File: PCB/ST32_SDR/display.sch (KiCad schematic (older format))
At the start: 1 part

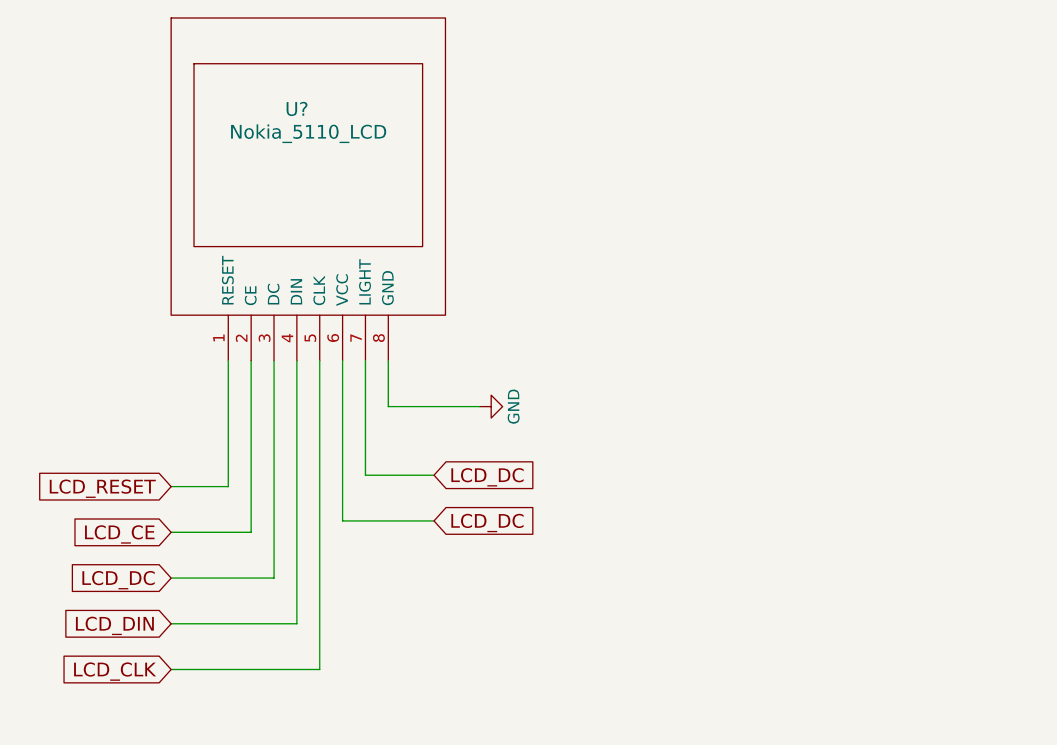
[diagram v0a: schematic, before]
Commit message: add LCD resistors
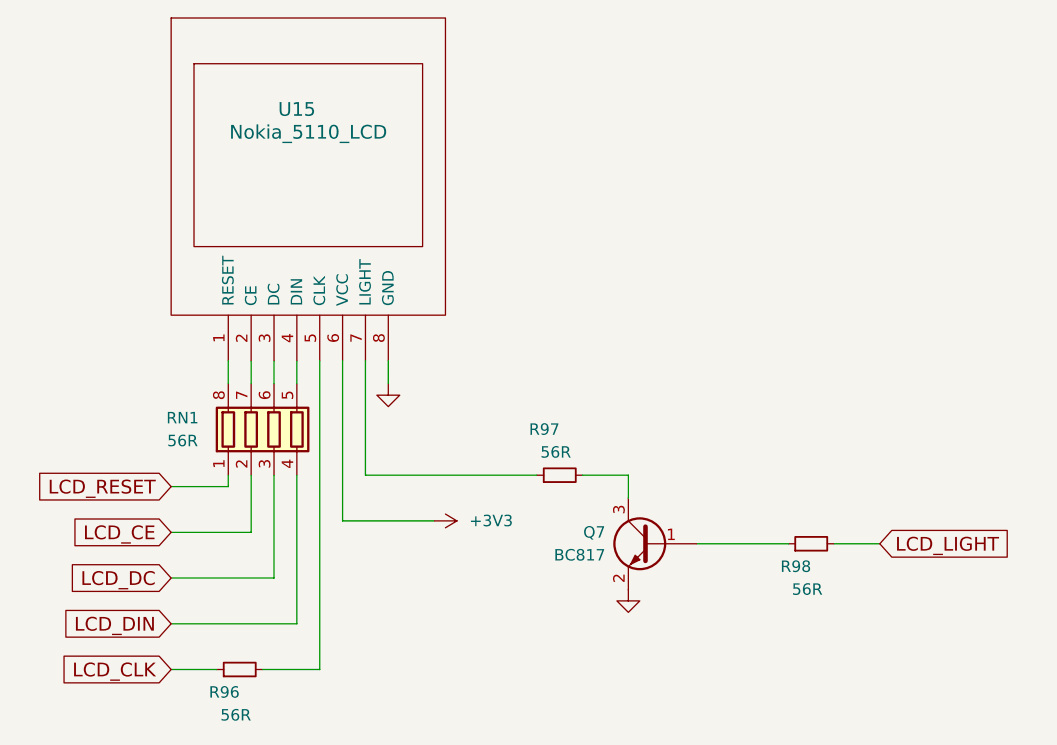
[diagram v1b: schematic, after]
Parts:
- added Q7: BC817, symbol Q_NPN_BEC
- added R96, R97, R98: 56R, symbol R_Small
- added RN1: 56R, symbol R_Pack04
- gave numbers to parts that had none: 1
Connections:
- net GND: now also Q7.2 (E)
- net LCD_CE: now also RN1.2 (R2.1); no longer U15.2 (CE)
- net LCD_CLK: now also R96.1; no longer U15.5 (CLK)
- net LCD_DC: now also RN1.3 (R3.1); no longer U15.3 (DC), U15.6 (VCC), U15.7 (LIGHT)
- net LCD_DIN: now also RN1.4 (R4.1); no longer U15.4 (DIN)
- net LCD_RESET: now also RN1.1 (R1.1); no longer U15.1 (RESET)
- new net: RN1.8 (R1.2), U15.1 (RESET)
- new net: RN1.7 (R2.2), U15.2 (CE)
- new net: RN1.6 (R3.2), U15.3 (DC)
- new net: RN1.5 (R4.2), U15.4 (DIN)
- new net: R96.2, U15.5 (CLK)
- new net: R97.1, U15.7 (LIGHT)
- new net: Q7.1 (B), R98.1
- new net: Q7.3 (C), R97.2
- new net +3V3: U15.6 (VCC)
- new net LCD_LIGHT: R98.2
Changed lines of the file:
@@
 $EndDescr
 $Comp
-L GND #PWR?
+L GND #PWR177
 U 1 1 5DDA30F6
-P 3900 2700
-F 0 "#PWR?" H 3900 2450 50  0001 C CNN
-F 1 "GND" H 3900 2550 50  0000 C CNN
-F 2 "" H 3900 2700 50  0001 C CNN
-F 3 "" H 3900 2700 50  0001 C CNN
-	1    3900 2700
-	0    -1   -1   0
+P 3500 2600
+F 0 "#PWR177" H 3500 2350 50  0001 C CNN
+F 1 "GND" H 3500 2450 50  0001 C CNN
+F 2 "" H 3500 2600 50  0001 C CNN
+F 3 "" H 3500 2600 50  0001 C CNN
+	1    3500 2600
+	1    0    0    -1
 $EndComp
 $Comp
-L Nokia_5110_LCD U?
+L Nokia_5110_LCD U15
 U 1 1 5DDA3747
 P 3150 1600
-F 0 "U?" H 3100 1800 60  0000 C CNN
+F 0 "U15" H 3100 1800 60  0000 C CNN
 F 1 "Nokia_5110_LCD" H 3150 1700 60  0000 C CNN
 F 2 "" H 2700 1400 60  0000 C CNN
@@
 	1    0    0    -1
 $EndComp
-Wire Wire Line
-	3500 2500 3500 2700
-Wire Wire Line
-	3500 2700 3900 2700
-Wire Wire Line
-	3000 2500 3000 3450
 Text GLabel 2550 3450 0    60   Input ~ 0
 LCD_DC
-Wire Wire Line
-	3000 3450 2550 3450
 Text GLabel 2550 3250 0    60   Input ~ 0
 LCD_CE
-Wire Wire Line
-	2550 3250 2900 3250
-Wire Wire Line
-	2900 3250 2900 2500
 Text GLabel 2550 3050 0    60   Input ~ 0
 LCD_RESET
+Text GLabel 2550 3650 0    60   Input ~ 0
+LCD_DIN
+Text GLabel 2550 3850 0    60   Input ~ 0
+LCD_CLK
+Text GLabel 5650 3300 2    60   Input ~ 0
+LCD_LIGHT
+$Comp
+L R_Pack04 RN1
+U 1 1 5DDA5123
+P 3000 2800
+F 0 "RN1" H 2600 2850 50  0000 C CNN
+F 1 "56R" H 2600 2750 50  0000 C CNN
+F 2 "" V 3275 2800 50  0001 C CNN
+F 3 "" H 3000 2800 50  0001 C CNN
+	1    3000 2800
+	1    0    0    -1
+$EndComp
+$Comp
+L +3V3 #PWR178
+U 1 1 5DDA52BE
+P 3700 3200
+F 0 "#PWR178" H 3700 3050 50  0001 C CNN
+F 1 "+3V3" V 3700 3450 50  0000 C CNN
+F 2 "" H 3700 3200 50  0001 C CNN
+F 3 "" H 3700 3200 50  0001 C CNN
+	1    3700 3200
+	0    1    1    0
+$EndComp
 Wire Wire Line
 	2550 3050 2800 3050
 Wire Wire Line
-	2800 3050 2800 2500
-Text GLabel 2550 3650 0    60   Input ~ 0
-LCD_DIN
-Wire Wire Line
 	2550 3650 3100 3650
-Wire Wire Line
-	3100 3650 3100 2500
-Text GLabel 2550 3850 0    60   Input ~ 0
-LCD_CLK
-Wire Wire Line
-	2550 3850 3200 3850
-Wire Wire Line
-	3200 3850 3200 2500
-Text GLabel 3700 3000 2    60   Input ~ 0
-LCD_DC
-Wire Wire Line
-	3700 3000 3400 3000
 Wire Wire Line
 	3400 3000 3400 2500
@@
 Wire Wire Line
 	3300 3200 3700 3200
-Text GLabel 3700 3200 2    60   Input ~ 0
-LCD_DC
+Wire Wire Line
+	3000 3450 2550 3450
+Wire Wire Line
+	2550 3250 2900 3250
+Wire Wire Line
+	2800 2600 2800 2500
+Wire Wire Line
+	2900 2500 2900 2600
+Wire Wire Line
+	3000 2500 3000 2600
+Wire Wire Line
+	3100 2500 3100 2600
+Wire Wire Line
+	3200 3850 3200 2500
+Wire Wire Line
+	2800 3050 2800 3000
+Wire Wire Line
+	2900 3250 2900 3000
+Wire Wire Line
+	3000 3450 3000 3000
+Wire Wire Line
+	3100 3650 3100 3000
+$Comp
+L R_Small R96
+U 1 1 5DDA5492
+P 2850 3850
+F 0 "R96" V 2750 3850 50  0000 L CNN
+F 1 "56R" V 2650 3800 50  0000 L CNN
+F 2 "" H 2850 3850 50  0001 C CNN
+F 3 "" H 2850 3850 50  0001 C CNN
+	1    2850 3850
+	0    -1   -1   0
+$EndComp
+Wire Wire Line
+	2950 3850 3200 3850
+Wire Wire Line
+	2750 3850 2550 3850
+$Comp
+L Q_NPN_BEC Q7
+U 1 1 5DDA55BA
+P 4650 3300
+F 0 "Q7" H 4850 3350 50  0000 L CNN
+F 1 "BC817" H 4850 3250 50  0000 L CNN
+F 2 "" H 4850 3400 50  0001 C CNN
+F 3 "" H 4650 3300 50  0001 C CNN
+	1    4650 3300
+	-1   0    0    -1
+$EndComp
+Wire Wire Line
+	4550 3000 4550 3100
+$Comp
+L R_Small R98
+U 1 1 5DDA5646
+P 5350 3300
+F 0 "R98" V 5250 3300 50  0000 L CNN
+F 1 "56R" V 5150 3250 50  0000 L CNN
+F 2 "" H 5350 3300 50  0001 C CNN
+F 3 "" H 5350 3300 50  0001 C CNN
+	1    5350 3300
+	0    -1   -1   0
+$EndComp
+Wire Wire Line
+	5450 3300 5650 3300
+Wire Wire Line
+	5250 3300 4850 3300
+$Comp
+L GND #PWR179
+U 1 1 5DDA5709
+P 4550 3500
+F 0 "#PWR179" H 4550 3250 50  0001 C CNN
+F 1 "GND" H 4550 3350 50  0001 C CNN
+F 2 "" H 4550 3500 50  0001 C CNN
+F 3 "" H 4550 3500 50  0001 C CNN
+	1    4550 3500
+	1    0    0    -1
+$EndComp
+Wire Wire Line
+	3500 2600 3500 2500
+$Comp
+L R_Small R97
+U 1 1 5DDA5830
+P 4250 3000
+F 0 "R97" V 4450 3000 50  0000 L CNN
+F 1 "56R" V 4350 2950 50  0000 L CNN
+F 2 "" H 4250 3000 50  0001 C CNN
+F 3 "" H 4250 3000 50  0001 C CNN
+	1    4250 3000
+	0    -1   -1   0
+$EndComp
+Wire Wire Line
+	4350 3000 4550 3000
+Wire Wire Line
+	4150 3000 3400 3000
 $EndSCHEMATC

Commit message: update schematics
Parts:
- added C22, C23, C24: 100nF, symbol C_Small
- added C31, C55, C68, C74: C_Small, symbol C_Small
- added J2: IDC10 Serial Wire, symbol Conn_02x05_Odd_Even
- added RN2, RN9: 4.7k, symbol R_Pack04
- added RN8: 47, symbol R_Pack04
- added SW1, SW2, SW3, SW4: SW_Push_Dual, symbol SW_Push_Dual
- added SW5: ENCODER, symbol Rotary_Encoder_Switch
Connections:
- net +3V3: now also J2.1 (Pin_1), RN2.5 (R4.2), RN2.6 (R3.2), RN2.7 (R2.2), RN2.8 (R1.2), RN9.5 (R4.2), RN9.6 (R3.2), RN9.7 (R2.2)
- net GND: now also C22.2, C23.2, C24.2, C31.2, C55.2, C68.2, C74.2, J2.3 (Pin_3), J2.5 (Pin_5), J2.9 (Pin_9), SW1.2, SW1.4, SW2.2, SW2.4, SW3.2, SW3.4, SW4.2, SW4.4, SW5.3 (B), SW5.5
- new net: J2.10 (Pin_10), RN8.4 (R4.1)
- new net: J2.2 (Pin_2), RN8.1 (R1.1)
- new net: J2.4 (Pin_4), RN8.2 (R2.1)
- new net: J2.6 (Pin_6), RN8.3 (R3.1)
- new net ENCODER_A: C22.1, RN9.3 (R3.1), SW5.1 (A)
- new net ENCODER_B: C23.1, RN9.2 (R2.1), SW5.2 (C)
- new net KEY_A: C31.1, RN2.1 (R1.1), SW1.1, SW1.3
- new net KEY_B: C55.1, RN2.2 (R2.1), SW2.1, SW2.3
- new net KEY_C: C68.1, RN2.3 (R3.1), SW3.1, SW3.3
- new net KEY_D: C74.1, RN2.4 (R4.1), SW4.1, SW4.3
- new net KEY_MENU: C24.1, RN9.4 (R4.1), SW5.4
- new net MCU_RESET: RN8.5 (R4.2)
- new net SWCLK: RN8.7 (R2.2)
- new net SWDIO: RN8.8 (R1.2)
- new net SWO: RN8.6 (R3.2)

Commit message: begin PCB
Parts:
- removed R96: 56R, symbol R_Small
- added R21: 56R, UI:R_1206_0603, symbol R_Small
- Q7: footprint (none) -> TO_SOT_Packages_SMD:SOT-23
- RN1, RN2, RN8, RN9: footprint (none) -> Resistors_SMD:R_Array_Convex_4x0603
- U15: footprint (none) -> UI:Nokia_5110-3310_LCD
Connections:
- net LCD_CLK: now also R21.1
- net at U15.5 (CLK): now also R21.2
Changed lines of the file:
@@
 LIBS:4ms-ic
 LIBS:Display
-LIBS:TRXklopik
-LIBS:stm32
-LIBS:switches
-LIBS:cmos4000
-LIBS:conn
+LIBS:Connector
+LIBS:Relay
 LIBS:LCSDR-cache
 EELAYER 25 0
@@
 F 0 "U15" H 3100 1800 60  0000 C CNN
 F 1 "Nokia_5110_LCD" H 3150 1700 60  0000 C CNN
-F 2 "" H 2700 1400 60  0000 C CNN
+F 2 "UI:Nokia_5110-3310_LCD" H 2700 1400 60  0001 C CNN
 F 3 "" H 2700 1400 60  0000 C CNN
 	1    3150 1600
@@
 F 0 "RN1" H 2600 2850 50  0000 C CNN
 F 1 "56R" H 2600 2750 50  0000 C CNN
-F 2 "" V 3275 2800 50  0001 C CNN
+F 2 "Resistors_SMD:R_Array_Convex_4x0603" V 3275 2800 50  0001 C CNN
 F 3 "" H 3000 2800 50  0001 C CNN
 	1    3000 2800
@@
 Wire Wire Line
 	3100 3650 3100 3000
-$Comp
-L R_Small R96
-U 1 1 5DDA5492
-P 2850 3850
-F 0 "R96" V 2750 3850 50  0000 L CNN
-F 1 "56R" V 2650 3800 50  0000 L CNN
-F 2 "" H 2850 3850 50  0001 C CNN
-F 3 "" H 2850 3850 50  0001 C CNN
-	1    2850 3850
-	0    -1   -1   0
-$EndComp
 Wire Wire Line
 	2950 3850 3200 3850
@@
 F 0 "Q7" H 4850 3350 50  0000 L CNN
 F 1 "BC817" H 4850 3250 50  0000 L CNN
-F 2 "" H 4850 3400 50  0001 C CNN
+F 2 "TO_SOT_Packages_SMD:SOT-23" H 4850 3400 50  0001 C CNN
 F 3 "" H 4650 3300 50  0001 C CNN
 	1    4650 3300
@@
 F 0 "RN2" H 8550 1500 50  0000 C CNN
 F 1 "4.7k" H 8550 1400 50  0000 C CNN
-F 2 "" V 9225 1450 50  0001 C CNN
+F 2 "Resistors_SMD:R_Array_Convex_4x0603" V 9225 1450 50  0001 C CNN
 F 3 "" H 8950 1450 50  0001 C CNN
 	1    8950 1450
@@
 F 0 "RN8" V 3700 6200 50  0000 C CNN
 F 1 "47" V 4200 6200 50  0000 C CNN
-F 2 "" V 4275 6200 50  0001 C CNN
+F 2 "Resistors_SMD:R_Array_Convex_4x0603" V 4275 6200 50  0001 C CNN
 F 3 "" H 4000 6200 50  0001 C CNN
 	1    4000 6200
@@
 F 0 "RN9" H 7250 5100 50  0000 C CNN
 F 1 "4.7k" H 7250 5000 50  0000 C CNN
-F 2 "" V 7925 5050 50  0001 C CNN
+F 2 "Resistors_SMD:R_Array_Convex_4x0603" V 7925 5050 50  0001 C CNN
 F 3 "" H 7650 5050 50  0001 C CNN
 	1    7650 5050
@@
 	1    0    0    -1
 $EndComp
+$Comp
+L R_Small R21
+U 1 1 5DDFD76F
+P 2850 3850
+F 0 "R21" V 2750 3850 50  0000 L CNN
+F 1 "56R" V 2650 3800 50  0000 L CNN
+F 2 "UI:R_1206_0603" H 2850 3850 50  0001 C CNN
+F 3 "" H 2850 3850 50  0001 C CNN
+	1    2850 3850
+	0    -1   -1   0
+$EndComp
 $EndSCHEMATC

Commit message: PCB update
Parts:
- C22, C23, C24, C31, C55, C68, C74: footprint (none) -> UI:C_1206_0603
- J2: footprint (none) -> UI:USBBLASTER
- R97, R98: footprint (none) -> UI:R_1206_0603
- SW1, SW2, SW3, SW4: footprint (none) -> Buttons_Switches_ThroughHole:SW_PUSH_6mm_h13mm
- SW5: footprint (none) -> UI:SF-ROTARY-ENCODER
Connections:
- net +3V3: now also RN9.8 (R1.2); no longer RN9.5 (R4.2)
- net ENCODER_A: now also RN9.2 (R2.1); no longer RN9.3 (R3.1)
- net ENCODER_B: now also RN9.3 (R3.1); no longer RN9.2 (R2.1)
- net KEY_A: now also RN2.4 (R4.1); no longer RN2.1 (R1.1)
- net KEY_B: now also RN2.3 (R3.1); no longer RN2.2 (R2.1)
- net KEY_C: now also RN2.2 (R2.1); no longer RN2.3 (R3.1)
- net KEY_D: now also RN2.1 (R1.1); no longer RN2.4 (R4.1)
- net KEY_MENU: now also RN9.1 (R1.1); no longer RN9.4 (R4.1)

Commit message: LCD at SPI3
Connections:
- net LCD_CE: now also RN1.7 (R2.2); no longer RN1.2 (R2.1)
- net LCD_DC: now also RN1.6 (R3.2); no longer RN1.3 (R3.1)
- net LCD_DIN: now also RN1.5 (R4.2); no longer RN1.4 (R4.1)
- net LCD_RESET: now also RN1.8 (R1.2); no longer RN1.1 (R1.1)
- net at U15.1 (RESET): now also RN1.1 (R1.1); no longer RN1.8 (R1.2)
- net at U15.2 (CE): now also RN1.2 (R2.1); no longer RN1.7 (R2.2)
- net at U15.3 (DC): now also RN1.3 (R3.1); no longer RN1.6 (R3.2)
- net at U15.4 (DIN): now also RN1.4 (R4.1); no longer RN1.5 (R4.2)
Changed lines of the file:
@@
 LIBS:4ms-ic
 LIBS:Display
-LIBS:Connector
-LIBS:Relay
+LIBS:switches
+LIBS:cmos4000
 LIBS:LCSDR-cache
 EELAYER 25 0
@@
 $EndDescr
 $Comp
-L GND #PWR53
+L GND #PWR051
 U 1 1 5DDA30F6
 P 3500 2600
-F 0 "#PWR53" H 3500 2350 50  0001 C CNN
+F 0 "#PWR051" H 3500 2350 50  0001 C CNN
 F 1 "GND" H 3500 2450 50  0001 C CNN
 F 2 "" H 3500 2600 50  0001 C CNN
@@
 U 1 1 5DDA5123
 P 3000 2800
-F 0 "RN1" H 2600 2850 50  0000 C CNN
-F 1 "56R" H 2600 2750 50  0000 C CNN
+F 0 "RN1" H 2600 2750 50  0000 C CNN
+F 1 "56R" H 2600 2850 50  0000 C CNN
 F 2 "Resistors_SMD:R_Array_Convex_4x0603" V 3275 2800 50  0001 C CNN
 F 3 "" H 3000 2800 50  0001 C CNN
 	1    3000 2800
-	1    0    0    -1
-$EndComp
-$Comp
-L +3V3 #PWR54
+	1    0    0    1
+$EndComp
+$Comp
+L +3V3 #PWR052
 U 1 1 5DDA52BE
 P 3700 3200
-F 0 "#PWR54" H 3700 3050 50  0001 C CNN
+F 0 "#PWR052" H 3700 3050 50  0001 C CNN
 F 1 "+3V3" V 3700 3450 50  0000 C CNN
 F 2 "" H 3700 3200 50  0001 C CNN
@@
 	5250 3300 4850 3300
 $Comp
-L GND #PWR55
+L GND #PWR053
 U 1 1 5DDA5709
 P 4550 3500
-F 0 "#PWR55" H 4550 3250 50  0001 C CNN
+F 0 "#PWR053" H 4550 3250 50  0001 C CNN
 F 1 "GND" H 4550 3350 50  0001 C CNN
 F 2 "" H 4550 3500 50  0001 C CNN
@@
 Connection ~ 8750 1750
 $Comp
-L GND #PWR67
+L GND #PWR054
 U 1 1 5DDE0799
 P 10250 1750
-F 0 "#PWR67" H 10250 1500 50  0001 C CNN
+F 0 "#PWR054" H 10250 1500 50  0001 C CNN
 F 1 "GND" H 10250 1600 50  0001 C CNN
 F 2 "" H 10250 1750 50  0001 C CNN
@@
 $EndComp
 $Comp
-L GND #PWR63
+L GND #PWR055
 U 1 1 5DDE0865
 P 9350 2000
-F 0 "#PWR63" H 9350 1750 50  0001 C CNN
+F 0 "#PWR055" H 9350 1750 50  0001 C CNN
 F 1 "GND" H 9350 1850 50  0001 C CNN
 F 2 "" H 9350 2000 50  0001 C CNN
@@
 $EndComp
 $Comp
-L GND #PWR69
+L GND #PWR056
 U 1 1 5DDE0A57
 P 10250 2450
-F 0 "#PWR69" H 10250 2200 50  0001 C CNN
+F 0 "#PWR056" H 10250 2200 50  0001 C CNN
 F 1 "GND" H 10250 2300 50  0001 C CNN
 F 2 "" H 10250 2450 50  0001 C CNN
@@
 $EndComp
 $Comp
-L GND #PWR64
+L GND #PWR057
 U 1 1 5DDE0BFA
 P 9350 2700
-F 0 "#PWR64" H 9350 2450 50  0001 C CNN
+F 0 "#PWR057" H 9350 2450 50  0001 C CNN
 F 1 "GND" H 9350 2550 50  0001 C CNN
 F 2 "" H 9350 2700 50  0001 C CNN
@@
 $EndComp
 $Comp
-L GND #PWR71
+L GND #PWR058
 U 1 1 5DDE0CF4
 P 10250 3150
-F 0 "#PWR71" H 10250 2900 50  0001 C CNN
+F 0 "#PWR058" H 10250 2900 50  0001 C CNN
 F 1 "GND" H 10250 3000 50  0001 C CNN
 F 2 "" H 10250 3150 50  0001 C CNN
@@
 $EndComp
 $Comp
-L GND #PWR65
+L GND #PWR059
 U 1 1 5DDE0D04
 P 9350 3400
-F 0 "#PWR65" H 9350 3150 50  0001 C CNN
+F 0 "#PWR059" H 9350 3150 50  0001 C CNN
 F 1 "GND" H 9350 3250 50  0001 C CNN
 F 2 "" H 9350 3400 50  0001 C CNN
@@
 $EndComp
 $Comp
-L GND #PWR73
+L GND #PWR060
 U 1 1 5DDE0F84
 P 10250 3850
-F 0 "#PWR73" H 10250 3600 50  0001 C CNN
+F 0 "#PWR060" H 10250 3600 50  0001 C CNN
 F 1 "GND" H 10250 3700 50  0001 C CNN
 F 2 "" H 10250 3850 50  0001 C CNN
@@
 $EndComp
 $Comp
-L GND #PWR66
+L GND #PWR061
 U 1 1 5DDE0F92
 P 9350 4100
-F 0 "#PWR66" H 9350 3850 50  0001 C CNN
+F 0 "#PWR061" H 9350 3850 50  0001 C CNN
 F 1 "GND" H 9350 3950 50  0001 C CNN
 F 2 "" H 9350 4100 50  0001 C CNN
@@
 Connection ~ 8850 1200
 $Comp
-L +3V3 #PWR61
+L +3V3 #PWR062
 U 1 1 5DDE1221
 P 8950 1050
-F 0 "#PWR61" H 8950 900 50  0001 C CNN
+F 0 "#PWR062" H 8950 900 50  0001 C CNN
 F 1 "+3V3" H 8950 1200 50  0000 C CNN
 F 2 "" H 8950 1050 50  0001 C CNN
@@
 Connection ~ 9750 3850
 $Comp
-L GND #PWR74
+L GND #PWR063
 U 1 1 5DDE176E
 P 10250 4050
-F 0 "#PWR74" H 10250 3800 50  0001 C CNN
+F 0 "#PWR063" H 10250 3800 50  0001 C CNN
 F 1 "GND" H 10250 3900 50  0001 C CNN
 F 2 "" H 10250 4050 50  0001 C CNN
@@
 $EndComp
 $Comp
-L GND #PWR72
+L GND #PWR064
 U 1 1 5DDE17A6
 P 10250 3350
-F 0 "#PWR72" H 10250 3100 50  0001 C CNN
+F 0 "#PWR064" H 10250 3100 50  0001 C CNN
 F 1 "GND" H 10250 3200 50  0001 C CNN
 F 2 "" H 10250 3350 50  0001 C CNN
@@
 $EndComp
 $Comp
-L GND #PWR70
+L GND #PWR065
 U 1 1 5DDE17FC
 P 10250 2650
-F 0 "#PWR70" H 10250 2400 50  0001 C CNN
+F 0 "#PWR065" H 10250 2400 50  0001 C CNN
 F 1 "GND" H 10250 2500 50  0001 C CNN
 F 2 "" H 10250 2650 50  0001 C CNN
@@
 $EndComp
 $Comp
-L GND #PWR68
+L GND #PWR066
 U 1 1 5DDE1834
 P 10250 1950
-F 0 "#PWR68" H 10250 1700 50  0001 C CNN
+F 0 "#PWR066" H 10250 1700 50  0001 C CNN
 F 1 "GND" H 10250 1800 50  0001 C CNN
 F 2 "" H 10250 1950 50  0001 C CNN
@@
 	4300 6450 4650 6450
 $Comp
-L GND #PWR52
+L GND #PWR067
 U 1 1 5DDE3D09
 P 2350 6450
-F 0 "#PWR52" H 2350 6200 50  0001 C CNN
+F 0 "#PWR067" H 2350 6200 50  0001 C CNN
 F 1 "GND" H 2350 6300 50  0001 C CNN
 F 2 "" H 2350 6450 50  0001 C CNN
@@
 Connection ~ 2350 6200
 $Comp
-L +3.3V #PWR51
+L +3.3V #PWR068
 U 1 1 5DDEF6A4
 P 2350 5900
-F 0 "#PWR51" H 2350 5750 50  0001 C CNN
+F 0 "#PWR068" H 2350 5750 50  0001 C CNN
 F 1 "+3.3V" H 2350 6040 50  0000 C CNN
 F 2 "" H 2350 5900 50  0001 C CNN
@@
 $EndComp
 $Comp
-L GND #PWR60
+L GND #PWR069
 U 1 1 5DDEFDCD
 P 8400 5750
-F 0 "#PWR60" H 8400 5500 50  0001 C CNN
+F 0 "#PWR069" H 8400 5500 50  0001 C CNN
 F 1 "GND" H 8400 5600 50  0001 C CNN
 F 2 "" H 8400 5750 50  0001 C CNN
@@
 	8400 5550 9450 5550
 $Comp
-L +3V3 #PWR58
+L +3V3 #PWR070
 U 1 1 5DDF0133
 P 7750 4750
-F 0 "#PWR58" H 7750 4600 50  0001 C CNN
+F 0 "#PWR070" H 7750 4600 50  0001 C CNN
 F 1 "+3V3" H 7750 4900 50  0000 C CNN
 F 2 "" H 7750 4750 50  0001 C CNN
@@
 Connection ~ 9050 5550
 $Comp
-L GND #PWR62
+L GND #PWR071
 U 1 1 5DDF04A0
 P 9050 5800
-F 0 "#PWR62" H 9050 5550 50  0001 C CNN
+F 0 "#PWR071" H 9050 5550 50  0001 C CNN
 F 1 "GND" H 9050 5650 50  0001 C CNN
 F 2 "" H 9050 5800 50  0001 C CNN
@@
 	7550 5750 6800 5750
 $Comp
-L GND #PWR59
+L GND #PWR072
 U 1 1 5DDF65E7
 P 7800 5750
-F 0 "#PWR59" H 7800 5500 50  0001 C CNN
+F 0 "#PWR072" H 7800 5500 50  0001 C CNN
 F 1 "GND" H 7800 5600 50  0001 C CNN
 F 2 "" H 7800 5750 50  0001 C CNN
@@
 Connection ~ 7550 5750
 $Comp
-L GND #PWR57
+L GND #PWR073
 U 1 1 5DDF6EA6
 P 7550 6250
-F 0 "#PWR57" H 7550 6000 50  0001 C CNN
+F 0 "#PWR073" H 7550 6000 50  0001 C CNN
 F 1 "GND" H 7550 6100 50  0001 C CNN
 F 2 "" H 7550 6250 50  0001 C CNN
@@
 Connection ~ 7000 5550
 $Comp
-L GND #PWR56
+L GND #PWR074
 U 1 1 5DDF7068
 P 7000 6250
-F 0 "#PWR56" H 7000 6000 50  0001 C CNN
+F 0 "#PWR074" H 7000 6000 50  0001 C CNN
 F 1 "GND" H 7000 6100 50  0001 C CNN
 F 2 "" H 7000 6250 50  0001 C CNN

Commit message: UI PCB linux 1
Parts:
- removed C31, C55, C68, C74: C_Small, UI:C_1206_0603, symbol C_Small
- removed R97, R98: 56R, UI:R_1206_0603, symbol R_Small
- added C10, C11, C12, C13, C9: 100nF, UI:C_1206_0603, symbol C_Small
- added R24, R25: 56R, UI:R_1206_0603, symbol R_Small
- added SW6: SW_Push_Dual, Buttons_Switches_ThroughHole:SW_PUSH_6mm_h13mm, symbol SW_Push_Dual
- Q7: footprint TO_SOT_Packages_SMD:SOT-23 -> TO_SOT_Packages_SMD:SOT-23_Handsoldering
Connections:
- net +3V3: now also RN9.5 (R4.2)
- net ENCODER_A: now also RN9.3 (R3.1); no longer RN9.2 (R2.1)
- net ENCODER_B: now also RN9.2 (R2.1); no longer RN9.3 (R3.1)
- net GND: now also C10.2, C11.2, C12.2, C13.2, C9.2, SW6.2, SW6.4
- net KEY_A: now also C9.1
- net KEY_B: now also C10.1
- net KEY_C: now also C11.1
- net KEY_D: now also C12.1
- net LCD_LIGHT: now also R25.2
- net at U15.7 (LIGHT): now also R24.1
- net at Q7.1 (B): now also R25.1
- net at Q7.3 (C): now also R24.2
- net KEY_E: now reaches RN9.4 (R4.1)
- net KEY_E: now also C13.1, SW6.1, SW6.3
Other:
- moved on the sheet: RN2, SW1, SW2, SW3, SW4
